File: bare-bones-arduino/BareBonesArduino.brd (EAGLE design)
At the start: 59.7 x 61 mm, 26 parts, among them J1 FTDI_FT232, J3 ANALOG_IN, J4 POWER, J5 DIGITAL(PWM), J6 DIGITAL(PWM), J7 POWER_JACK, U1 328P, U2 LM7805CT, U3 LM1117T-3.3, Y1 16MHz

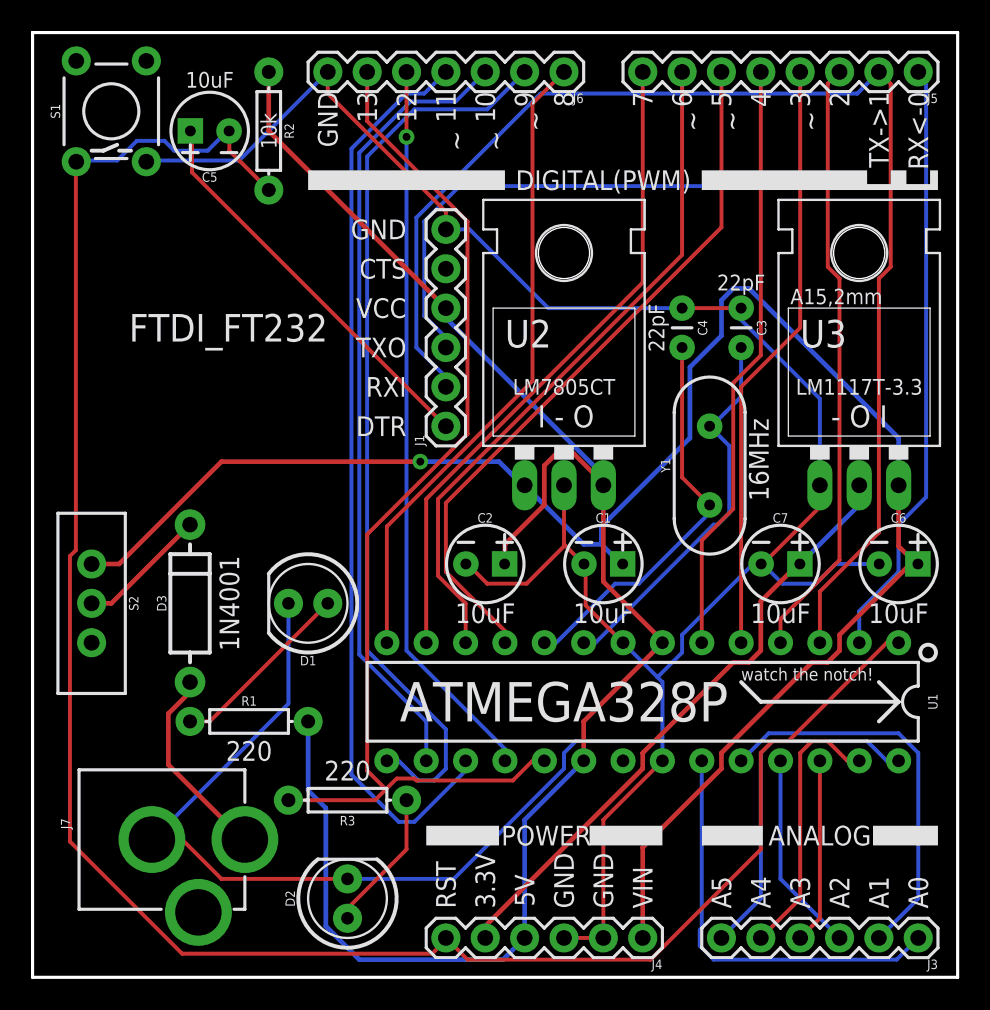
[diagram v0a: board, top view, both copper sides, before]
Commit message: Reposition components BareBonesArduino
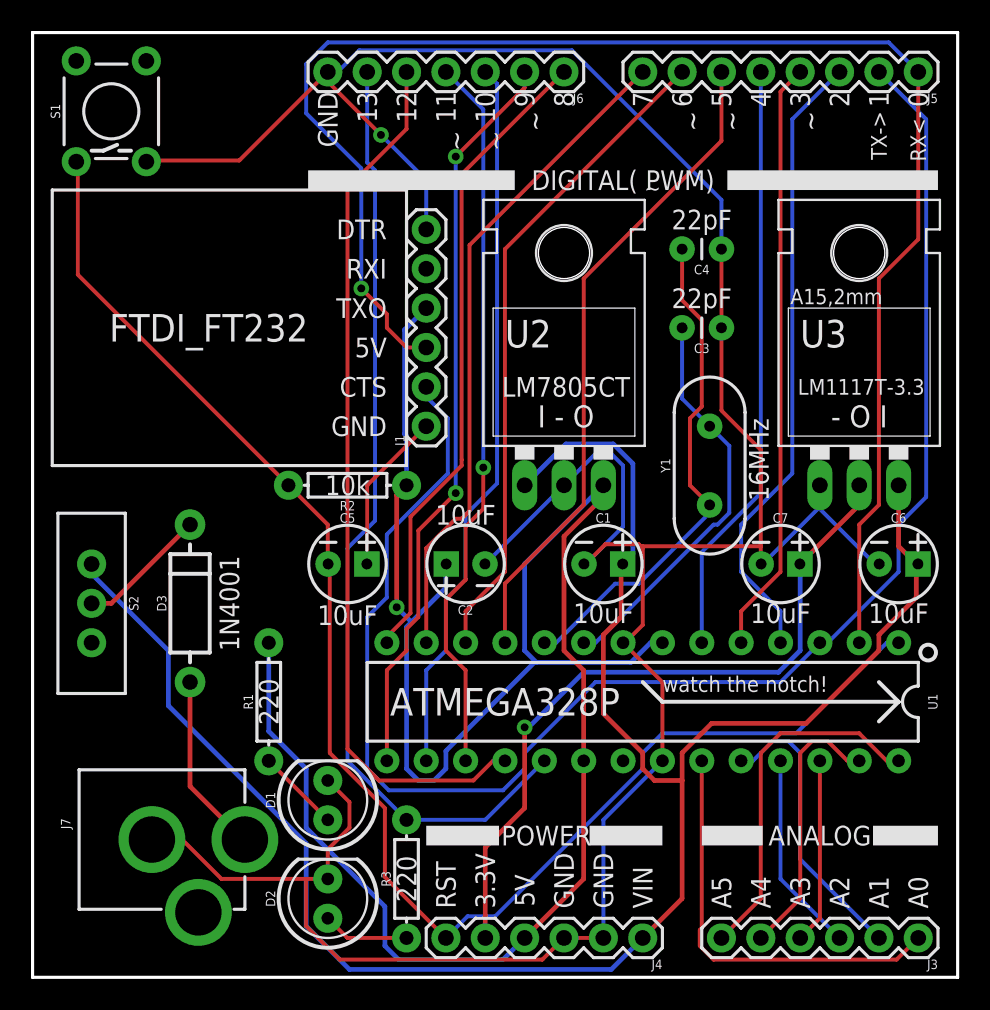
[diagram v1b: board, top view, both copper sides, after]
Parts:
- moved C5 29.3 mm to (20.3, 26.7), turned to 0 degrees
- moved R2 23.4 mm to (20.3, 31.8), turned to 180 degrees
- moved D1 12.8 mm to (19.1, 11.4), turned to 90 degrees
- moved R3 6.35 mm to (24.1, 6.35), turned to 90 degrees
- moved C4 5.24 mm to (43.2, 47.0), turned to 180 degrees
- moved C3 2.54 mm to (43.2, 41.9), turned to 180 degrees
- moved FRAME1 1.80 mm to (0.00, -7.62)
- moved R1 1.80 mm to (15.2, 17.8), turned to 90 degrees
- moved J1 1.27 mm to (25.4, 35.6)
- moved C2 1.27 mm to (27.9, 26.7), turned to 180 degrees
- moved D2 1.27 mm to (19.1, 5.08)
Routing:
- net RESET: track 129.8 -> 97.8 mm
- net VCC: track 110.5 -> 135.8 mm, vias 0 -> 1
- net D0(RX): track 80.9 -> 101.5 mm, vias 0 -> 1
- net D1(TX): track 84.5 -> 102.9 mm
- net DTR: track 25.9 -> 10.5 mm
- net D11(PWM): track 59.2 -> 47.0 mm, vias 0 -> 1
- net VIN: track 115.6 -> 126.6 mm, vias 1 -> 0
- net D9(PWM): track 58.7 -> 48.1 mm, vias 0 -> 2
- net GND: track 189.1 -> 198.9 mm, vias 0 -> 1
- net D12: track 47.1 -> 56.8 mm, vias 1 -> 0
- net D13(LED): track 69.8 -> 61.3 mm
- net A1: track 25.7 -> 18.7 mm
- net XTAL2: track 25.5 -> 32.5 mm
- net 3.3V: track 39.9 -> 46.8 mm, vias 0 -> 1
- net N$3: track 12.0 -> 5.39 mm
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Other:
- board text added: "0"
- board text added: "1"
- board text added: "DIGITAL( PWM)"
- board text added: "RX<-"
- board text added: "TX->"
- board text removed: "DIGITAL(PWM)"
- board text removed: "RX<-0"
- board text removed: "TX->1"
- board text removed: "VCC"
